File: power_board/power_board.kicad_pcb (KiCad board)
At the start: 2 copper layers, 66 x 54 mm, 59 parts, among them J1 Conn_01x02_Pin, J2 I2C, J3 12V_Out, Q1 NTMFS5C430NLT1G, SW1 SW_SPDT, U1 TPS54560BDDA, U2 TPS54560BDDA, U3 ADC081C021CIMM

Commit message: feat: 10A converters
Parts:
- removed C21: 100n, Capacitor_SMD:C_0805_2012Metric
- removed C22: 4.7u, Capacitor_SMD:C_0805_2012Metric
- removed C23: 150u, Capacitor_SMD:CP_Elec_6.3x7.7
- removed D2: B560C, Diode_SMD:D_SMC
- removed D3: LED, LED_SMD:LED_1206_3216Metric
- removed R16, R17, R18: 10k, Resistor_SMD:R_1206_3216Metric
- removed R19: 80, Resistor_SMD:R_1206_3216Metric
- added J4: I2C, Connector_JST:JST_EH_S5B-EH_1x05_P2.50mm_Horizontal, F.Cu at (131.5, 87.5)
- added NT1: NetTie_2, NetTie:NetTie-2_SMD_Pad0.5mm, B.Cu at (122.0, 105.5)
- C1: value 2.2u -> 150u; footprint Capacitor_SMD:C_0805_2012Metric -> Capacitor_SMD:CP_Elec_6.3x7.7
- C10, C8, C9: value 47u -> 22u; footprint Capacitor_SMD:C_1206_3216Metric -> Capacitor_SMD:C_0805_2012Metric
- C11: value 2.2u -> 22u
- C12, C14, C4: value 2.2u -> 100n
- C13: value 2.2u -> 22n
- C15: value 100n -> 33p
- C16: value 8.2n -> 10u
- C17: value 30p -> 10u
- C18: value 47u -> 10u; footprint Capacitor_SMD:C_1206_3216Metric -> Capacitor_SMD:C_0805_2012Metric
- C19: value 47u -> 100n; footprint Capacitor_SMD:C_1206_3216Metric -> Capacitor_SMD:C_0805_2012Metric
- C2, C3: value 2.2u -> 10u
- C20: value 47u -> 4.7u; footprint Capacitor_SMD:C_1206_3216Metric -> Capacitor_SMD:C_0805_2012Metric
- C5: value 100n -> 22n
- C6: value 4.7n -> 100n
- C7: value 47p -> 150p
- D1: value B560C -> LED; footprint Diode_SMD:D_SMC -> LED_SMD:LED_1206_3216Metric
- J2: value I2C -> Conn_01x02_Socket; footprint Connector_JST:JST_EH_S5B-EH_1x05_P2.50mm_Horizontal -> Connector_AMASS:AMASS_XT30PW-F_1x02_P2.50mm_Horizontal
- J3: value 12V_Out -> Conn_01x02_Socket
- L1: value 10u -> 3.3u; footprint Inductor_SMD:L_TechFuse_SL1250 -> Inductor_SMD:L_APV_APH1030
- L2: value 22u -> 6.8u; footprint Inductor_SMD:L_TechFuse_SL1250 -> Inductor_SMD:L_TaiTech_TMPC1265_13.5x12.5mm
- R1: value 150k -> 115k
- R10: value 26.1k -> 10k
- R11: value 140k -> 10k; footprint Resistor_SMD:R_0805_2012Metric -> Resistor_SMD:R_1206_3216Metric
- R12, R14: footprint Resistor_SMD:R_0805_2012Metric -> Resistor_SMD:R_1206_3216Metric
- R13: value 39k -> 10k; footprint Resistor_SMD:R_0805_2012Metric -> Resistor_SMD:R_1206_3216Metric
- R15: value 10k -> 80
- R2, R8: value 15k -> 10k
- R3: value 243k -> 52.3k
- R4: value 16.9k -> 73.2k
- R5: value 52.3k -> 10k
- R6: value 10k -> 52.3k
- R7: value 150k -> 191k
- R9: value 243k -> 39k
- U1, U2: value TPS54560BDDA -> TPS56A37RPAR; footprint Package_SO:Texas_R-PDSO-G8_EP2.95x4.9mm_Mask2.4x3.1mm_ThermalVias -> footprints:RPA0010A-MFG
- moved R15 38.7 mm to (115.5, 87.0), turned to 90 degrees
- moved C8 37.5 mm to (113.5, 98.3), turned to 90 degrees
- moved C10 36.3 mm to (114.5, 102.5)
- moved C9 34.6 mm to (115.5, 98.3), turned to 90 degrees
- moved D1 32.7 mm to (113.0, 87.0), turned to 90 degrees
- moved C18 30.6 mm to (115.5, 109.5), turned to 90 degrees
- moved C16 30.0 mm to (111.5, 109.5), turned to 90 degrees
- moved C17 27.3 mm to (113.5, 109.5), turned to 90 degrees
- moved R6 25.0 mm to (118.5, 108.5), turned to 0 degrees
- moved U2 21.1 mm to (118.0, 103.3), turned to 90 degrees
- moved C1 20.3 mm to (108.5, 96.0), turned to 90 degrees
- moved R9 19.2 mm to (143.0, 109.4)
- moved R1 19.1 mm to (109.5, 102.4)
- moved C4 18.3 mm to (114.5, 95.5)
- moved C7 18.3 mm to (118.5, 95.5), turned to 180 degrees
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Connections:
- C1 pad 2: GND -> PGND
- C10 pad 1: +5V -> +BATT
- C10 pad 2: GND -> PGND
- C11 pad 2: GND -> PGND
- C12 pad 2: GND -> PGND
- C13 pad 1: +BATT -> Net-(U2-SS)
- C13 pad 2: GND -> AGND
- C14 pad 1: +BATT -> Net-(U2-SW)
- C14 pad 2: GND -> Net-(U2-BOOT)
- C15 pad 1: Net-(D2-K) -> +12V
- C15 pad 2: Net-(U2-BOOT) -> Net-(U2-FB)
- C16 pad 1: Net-(C16-Pad1) -> +12V
- C16 pad 2: GND -> PGND
- C17 pad 1: Net-(U2-COMP) -> +12V
- C17 pad 2: GND -> PGND
- C18 pad 2: GND -> PGND
- C19 pad 1: +12V -> PGND
- C19 pad 2: GND -> Net-(U3-VIN)
- C2 pad 2: GND -> PGND
- C20 pad 1: +12V -> +3V3
- C20 pad 2: GND -> PGND
- C3 pad 2: GND -> PGND
- C4 pad 2: GND -> PGND
- C5 pad 1: Net-(D1-K) -> Net-(U1-SS)
- C5 pad 2: Net-(U1-BOOT) -> AGND
- C6 pad 1: Net-(C6-Pad1) -> Net-(U1-SW)
- C6 pad 2: GND -> Net-(U1-BOOT)
- C7 pad 1: Net-(U1-COMP) -> +5V
- C7 pad 2: GND -> Net-(U1-FB)
- C8 pad 2: GND -> PGND
- C9 pad 2: GND -> PGND
- D1 pad 1: Net-(D1-K) -> PGND
- D1 pad 2: GND -> Net-(D1-A)
- J2 pad 2: +3V3 -> PGND
- J3 pad 2: GND -> PGND
- L1 pad 1: Net-(D1-K) -> Net-(U1-SW)
- L2 pad 1: Net-(D2-K) -> Net-(U2-SW)
- Q1 pad 1: GND -> PGND
- Q1 pad 2: GND -> PGND
- Q1 pad 3: GND -> PGND
- R1 pad 2: Net-(U1-EN) -> /EN
- R10 pad 1: Net-(U2-COMP) -> Net-(U3-VIN)
- R10 pad 2: Net-(C16-Pad1) -> PGND
- R11 pad 1: Net-(D2-K) -> +3V3
- R11 pad 2: Net-(U2-FB) -> /ADR1
- R12 pad 1: Net-(U2-FB) -> /ADR1
- R12 pad 2: GND -> PGND
- R13 pad 1: +BATT -> +3V3
- R13 pad 2: Net-(U3-VIN) -> /ADR0
- R14 pad 1: Net-(U3-VIN) -> /ADR0
- R14 pad 2: GND -> PGND
- R15 pad 1: +3V3 -> +5V
- R15 pad 2: /ADR1 -> Net-(D1-A)
- R2 pad 1: Net-(U1-EN) -> /EN
- R2 pad 2: GND -> AGND
- R3 pad 1: Net-(U1-RT/CLK) -> Net-(U1-MODE)
- R3 pad 2: GND -> AGND
- R4 pad 1: Net-(U1-COMP) -> +5V
- R4 pad 2: Net-(C6-Pad1) -> Net-(U1-FB)
- R5 pad 1: Net-(D1-K) -> Net-(U1-FB)
- R5 pad 2: Net-(U1-FB) -> AGND
- R6 pad 1: Net-(U1-FB) -> Net-(U2-MODE)
- R6 pad 2: GND -> AGND
- R7 pad 1: +BATT -> +12V
- R7 pad 2: Net-(U2-EN) -> Net-(U2-FB)
- R8 pad 1: Net-(U2-EN) -> Net-(U2-FB)
- R8 pad 2: GND -> AGND
- R9 pad 1: Net-(U2-RT/CLK) -> +BATT
- R9 pad 2: GND -> Net-(U3-VIN)
- U1 pad 1: Net-(U1-BOOT) -> /EN
- U1 pad 2: +BATT -> Net-(U1-FB)
- U1 pad 3: Net-(U1-EN) -> AGND
- U1 pad 4: Net-(U1-RT/CLK) -> unconnected-(U1-PG-Pad4)
- U1 pad 5: Net-(U1-FB) -> Net-(U1-SS)
- U1 pad 6: Net-(U1-COMP) -> Net-(U1-SW)
- U1 pad 7: GND -> Net-(U1-BOOT)
- U1 pad 8: Net-(D1-K) -> +BATT
- U1 pad 9: GND -> PGND
- U2 pad 1: Net-(U2-BOOT) -> /EN
- U2 pad 2: +BATT -> Net-(U2-FB)
- U2 pad 3: Net-(U2-EN) -> AGND
- U2 pad 4: Net-(U2-RT/CLK) -> unconnected-(U2-PG-Pad4)
- U2 pad 5: Net-(U2-FB) -> Net-(U2-SS)
- U2 pad 6: Net-(U2-COMP) -> Net-(U2-SW)
- U2 pad 7: GND -> Net-(U2-BOOT)
- U2 pad 8: Net-(D2-K) -> +BATT
- U2 pad 9: GND -> PGND
- U3 pad 7: GND -> PGND
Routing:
- net GND: track 104.1 -> 0.00 mm, vias 12 -> 0
- net AGND: track 0.00 -> 52.1 mm, vias 0 -> 3
- net PGND: track 0.00 -> 48.5 mm, vias 0 -> 9
- net +BATT: track 98.3 -> 54.9 mm, vias 0 -> 1
- net +5V: track 38.3 -> 76.4 mm, vias 1 -> 2
- net +12V: track 19.9 -> 48.4 mm, vias 0 -> 2
- net Net-(D1-K): track 22.6 -> 0.00 mm
- net Net-(D2-K): track 22.2 -> 0.00 mm
- net /EN: track 0.00 -> 20.4 mm, vias 0 -> 3
- net Net-(U3-VIN): track 10.4 -> 25.4 mm
- net Net-(U2-SW): track 0.00 -> 13.8 mm
- net /ADR0: track 28.3 -> 14.7 mm
- net Net-(U1-SW): track 0.00 -> 10.5 mm
- net Net-(U2-COMP): track 8.70 -> 0.00 mm, vias 2 -> 0
- net Net-(Q1-G): track 3.77 -> 12.0 mm
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- added copper zone on F.Cu, net +BATT
- added copper zone on B.Cu, net PGND
- removed copper zone on B.Cu, net GND
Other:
- board size 66 x 54 mm -> 73.5 x 41.5 mm
- board text added: "+"
- board text added: "-"
- board text added: "3V3"
- board text added: "5V"
- board text added: "CosplayCore"
- board text added: "Data"
- board text added: "Power Board V1.0"
- board text removed: "+3V3"
- board text removed: "+5V"
- board text removed: "5V + I2C"
- board text removed: "C1-4"
- board text removed: "C11-14"
- board text removed: "C18-20"
- board text removed: "C8-10"
- board text removed: "CosplayCore Power Board V1.0"
- board text removed: "Dat"
- board text removed: "I2C Address Selector"

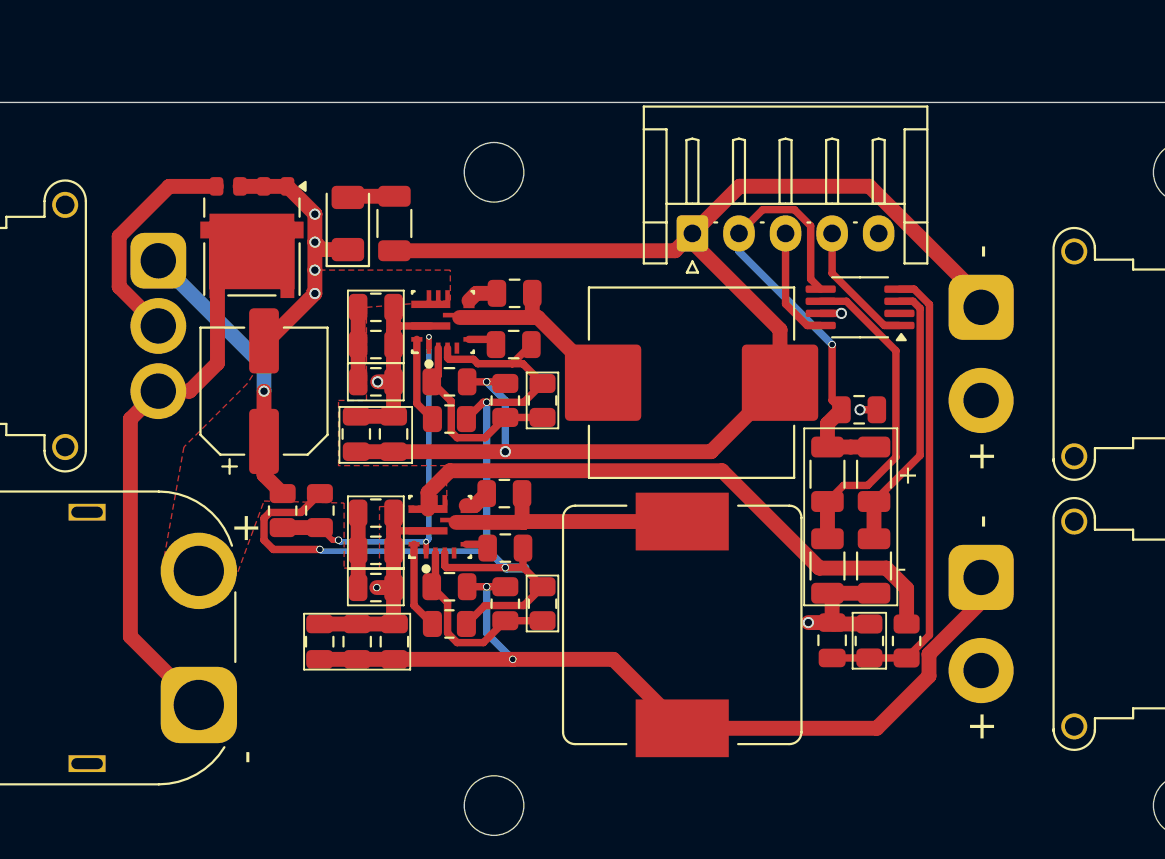
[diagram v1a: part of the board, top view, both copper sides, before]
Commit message: larger power traces
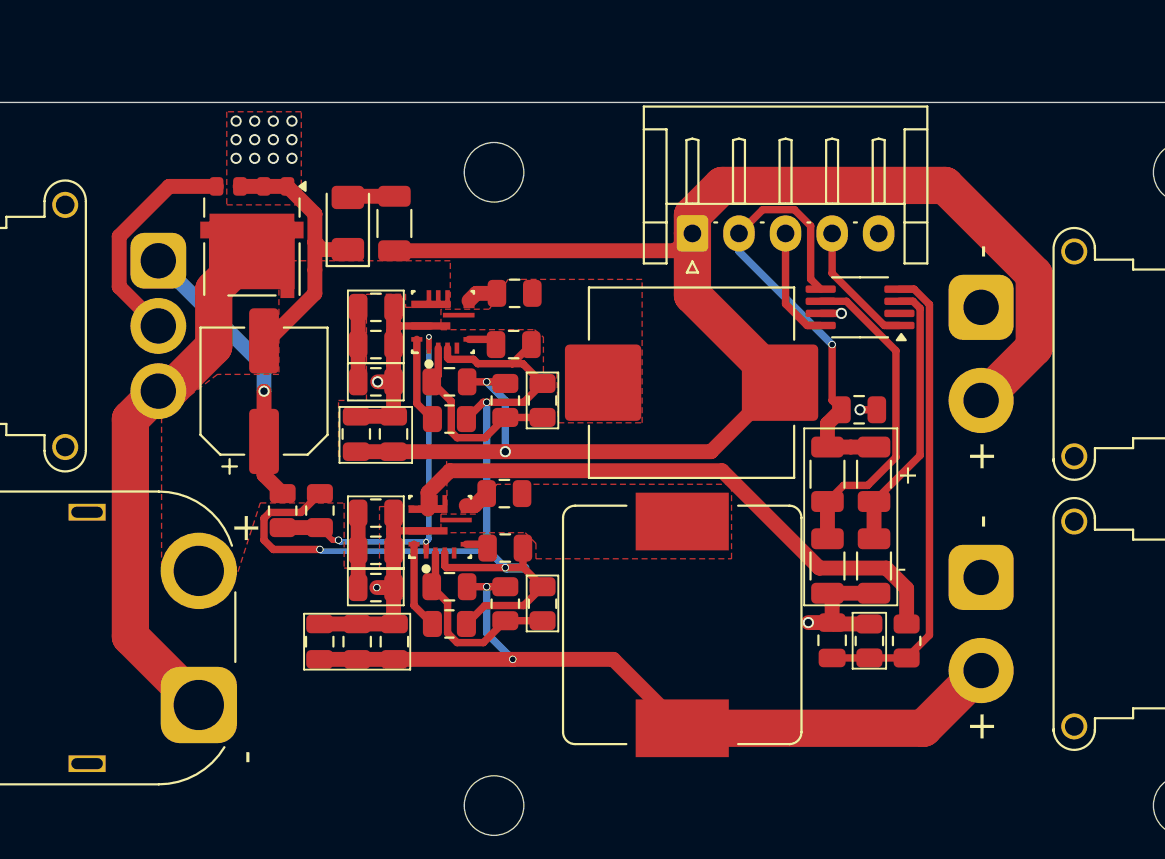
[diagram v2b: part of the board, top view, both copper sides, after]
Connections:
- J2 pad 1: +5V -> PGND
- J2 pad 2: PGND -> +5V
- J3 pad 1: +12V -> PGND
- J3 pad 2: PGND -> +12V
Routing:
- net Net-(U2-SW): track 13.8 -> 0.00 mm
- net Net-(U1-SW): track 10.5 -> 0.00 mm
- net +5V: track 76.4 -> 86.8 mm
- net +12V: track 48.4 -> 44.9 mm
- net Net-(J1-Pin_1): track 29.6 -> 28.9 mm
- net PGND: vias 9 -> 17
- added copper zone on F.Cu, net Net-(U1-SW)
- added copper zone on F.Cu, net Net-(U2-SW)
- added copper zone on F.Cu, net PGND

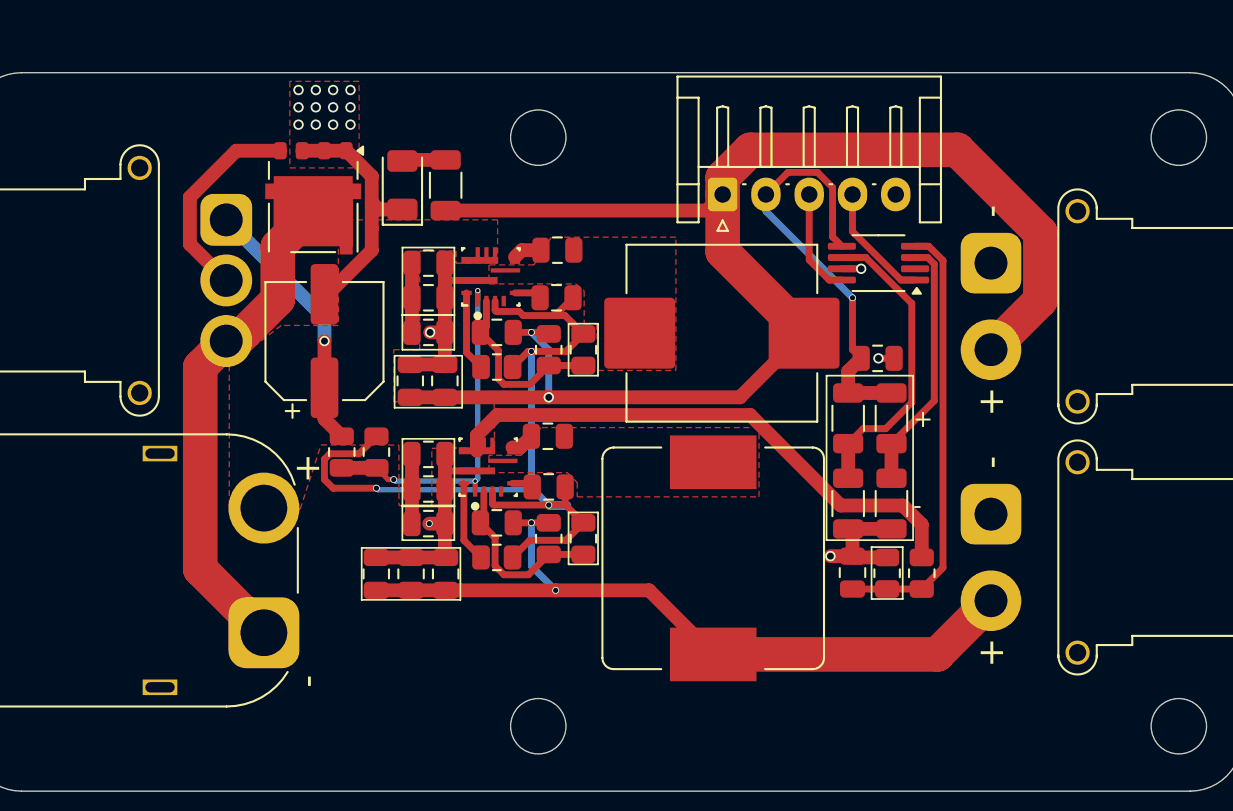
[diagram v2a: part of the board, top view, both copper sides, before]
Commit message: improve power fill thickness
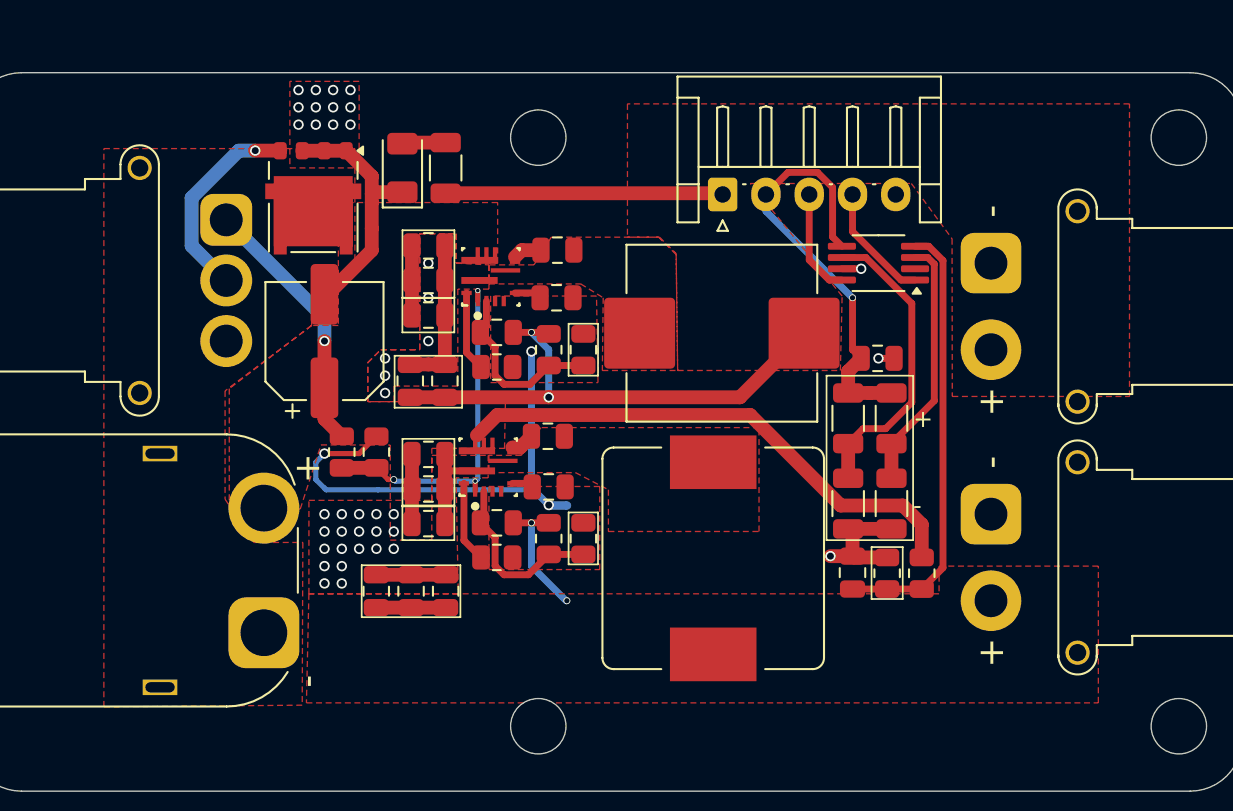
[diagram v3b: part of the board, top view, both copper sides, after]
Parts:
- moved C16 1.00 mm to (111.5, 110.5)
- moved C17 1.00 mm to (113.5, 110.5)
- moved C18 1.00 mm to (115.5, 110.5)
- moved C2 1.00 mm to (114.5, 90.5)
- moved C3 1.00 mm to (114.5, 92.5)
- moved C4 1.00 mm to (114.5, 94.5)
- moved D1 1.00 mm to (113.0, 86.0)
- moved R15 1.00 mm to (115.5, 86.0)
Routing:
- net +5V: track 86.8 -> 46.6 mm
- net +12V: track 44.9 -> 11.4 mm
- net Net-(J1-Pin_1): track 28.9 -> 0.00 mm
- net AGND: track 52.1 -> 28.1 mm
- net PGND: track 48.5 -> 42.8 mm, vias 17 -> 40
- net +BATT: track 54.9 -> 54.0 mm
- net Net-(Q1-G): track 12.0 -> 11.9 mm, vias 0 -> 1
- added copper zone on F.Cu, net +12V
- added copper zone on F.Cu, net +5V
- added copper zone on F.Cu, net AGND
- added copper zone on F.Cu, net Net-(J1-Pin_1)
